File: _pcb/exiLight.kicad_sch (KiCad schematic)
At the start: 49 parts, among them J1 Conn_01x04

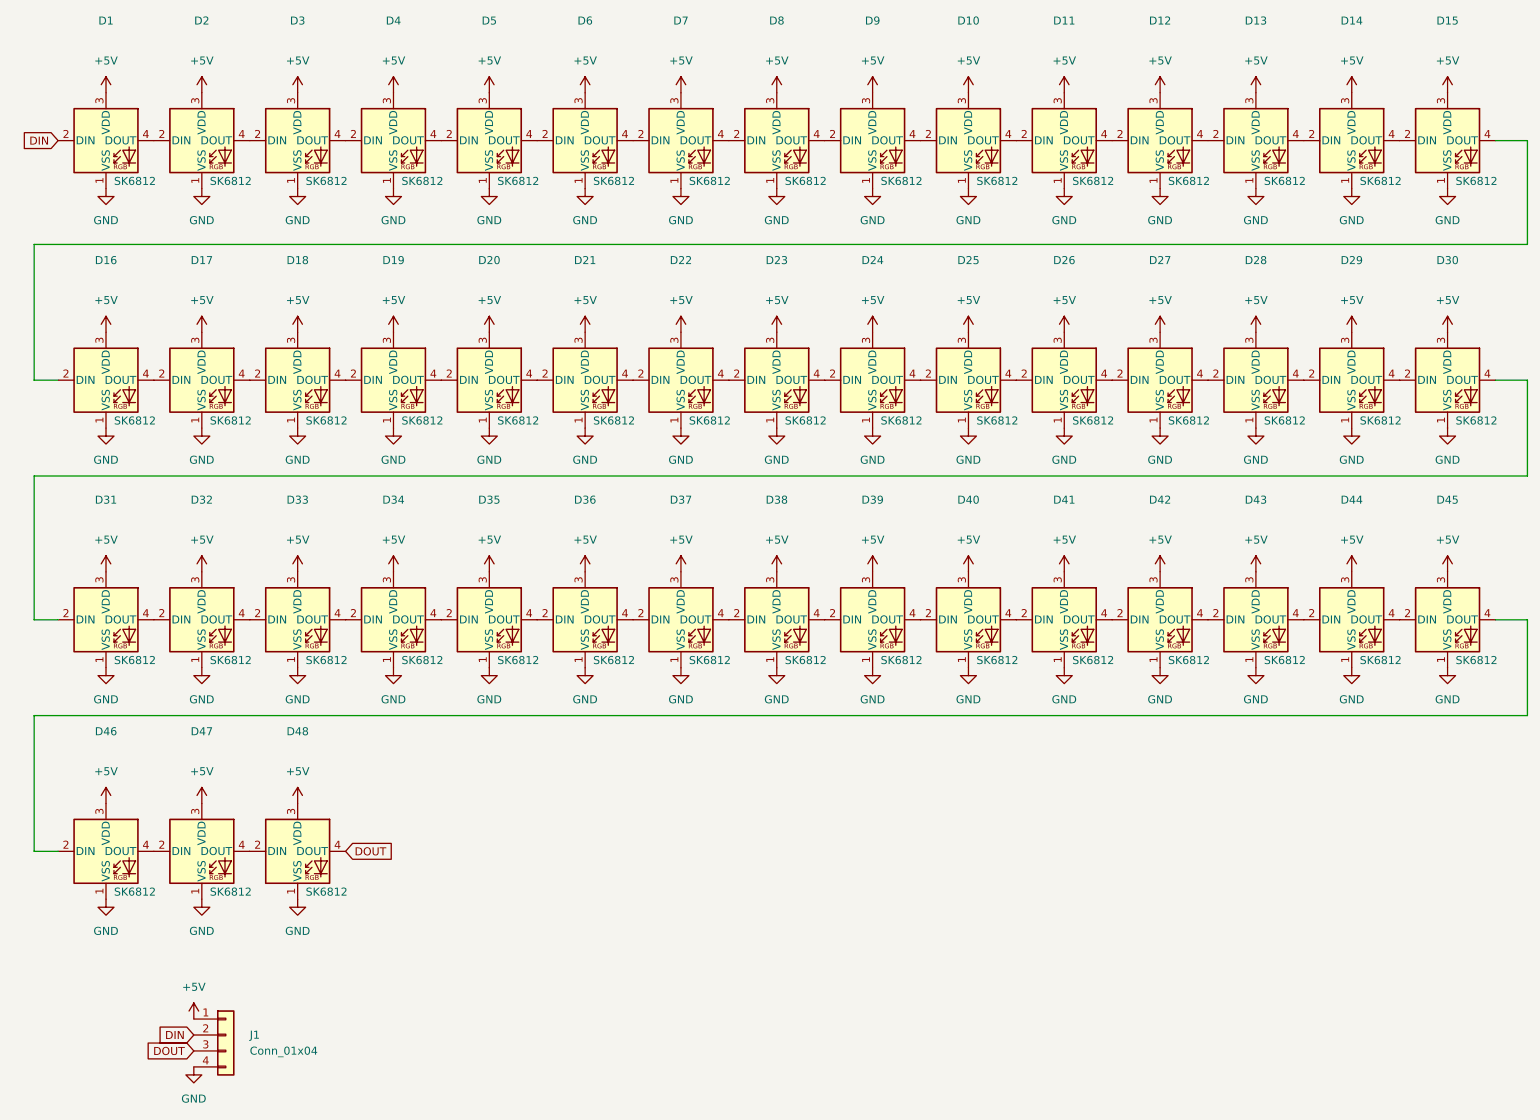
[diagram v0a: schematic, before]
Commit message: Added Caps
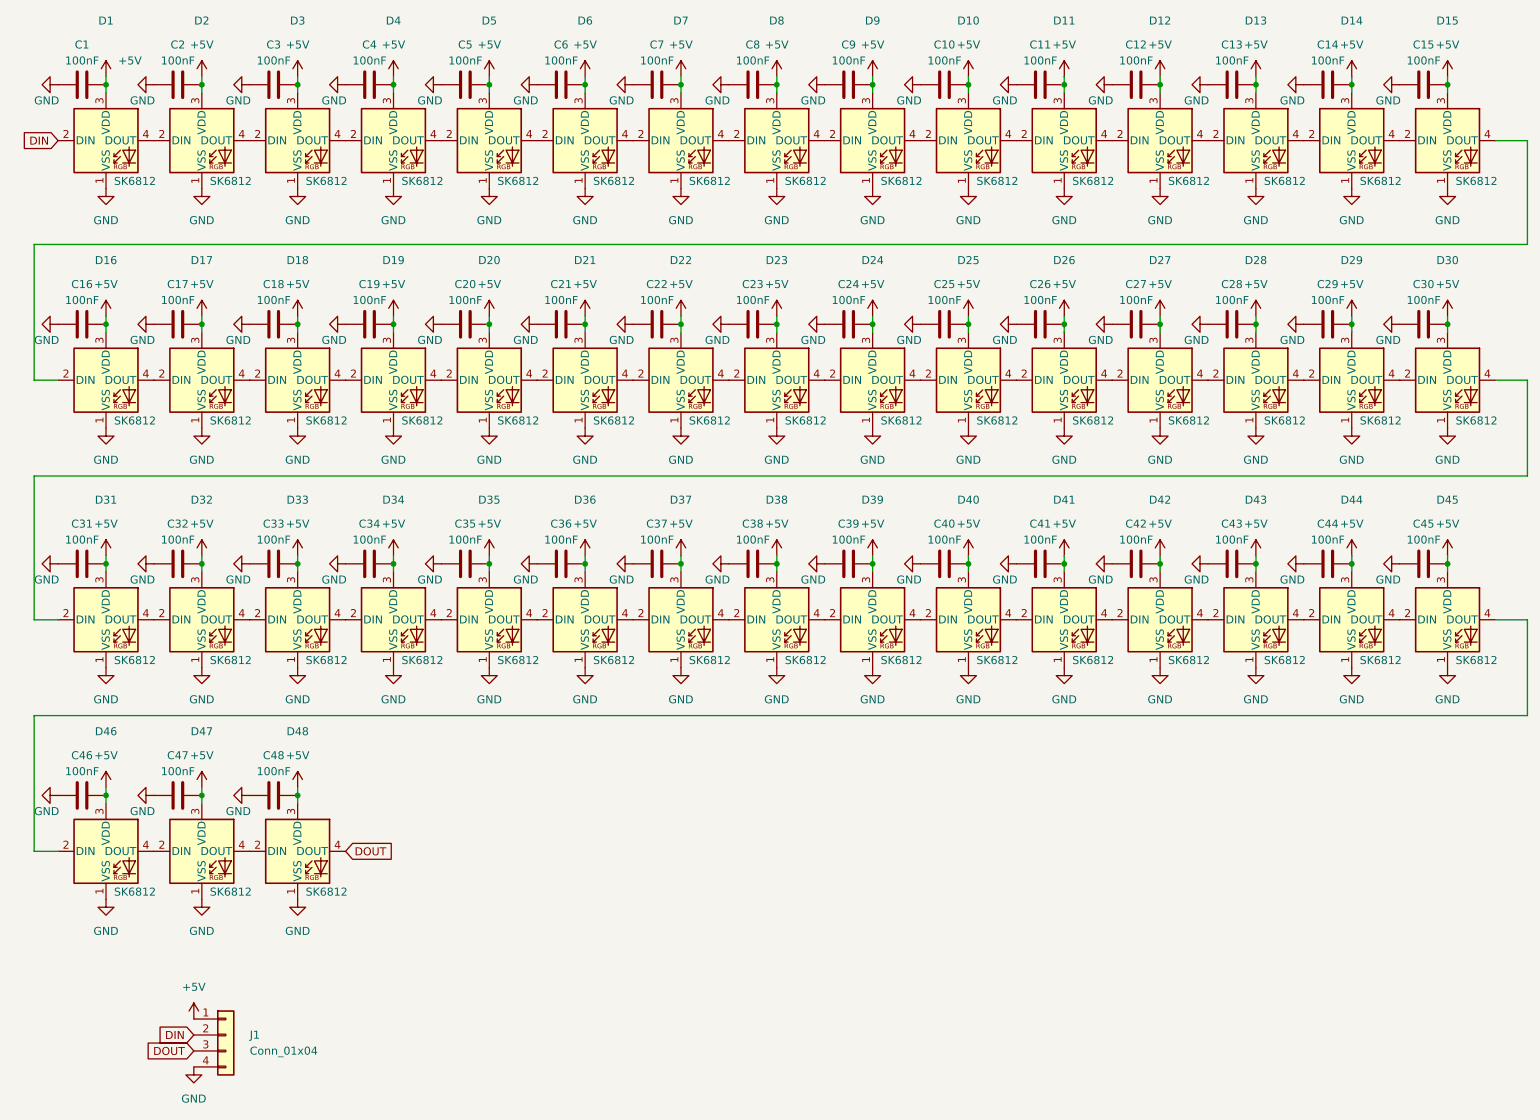
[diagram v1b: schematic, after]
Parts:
- added C1, C10, C11, C12, C13, C14, C15, C16, C17, C18, C19, C2, C20, C21, C22, C23, C24, C25, C26, C27, C28, C29, C3, C30, C31, C32, C33, C34, C35, C36, C37, C38, C39, C4, C40, C41, C42, C43, C44, C45, C46, C47, C48, C5, C6, C7, C8, C9: 100nF, Capacitor_SMD:C_0805_2012Metric_Pad1.18x1.45mm_HandSolder, symbol Device:C
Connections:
- net +5V: now also C1.2, C10.2, C11.2, C12.2, C13.2, C14.2, C15.2, C16.2, C17.2, C18.2, C19.2, C2.2, C20.2, C21.2, C22.2, C23.2, C24.2, C25.2, C26.2, C27.2, C28.2, C29.2, C3.2, C30.2, C31.2, C32.2, C33.2, C34.2, C35.2, C36.2, C37.2, C38.2, C39.2, C4.2, C40.2, C41.2, C42.2, C43.2, C44.2, C45.2, C46.2, C47.2, C48.2, C5.2, C6.2, C7.2, C8.2, C9.2
- net GND: now also C1.1, C10.1, C11.1, C12.1, C13.1, C14.1, C15.1, C16.1, C17.1, C18.1, C19.1, C2.1, C20.1, C21.1, C22.1, C23.1, C24.1, C25.1, C26.1, C27.1, C28.1, C29.1, C3.1, C30.1, C31.1, C32.1, C33.1, C34.1, C35.1, C36.1, C37.1, C38.1, C39.1, C4.1, C40.1, C41.1, C42.1, C43.1, C44.1, C45.1, C46.1, C47.1, C48.1, C5.1, C6.1, C7.1, C8.1, C9.1
